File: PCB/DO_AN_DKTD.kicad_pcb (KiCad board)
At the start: 2 copper layers, 96 x 97.2 mm, 147 parts, among them IC1 RTC_DS3231M, J10 Jack-DC, J11 Conn_01x03_Pin, J12 Micro_SD_Card_Det1, J2 Conn_01x02, J3 Conn_01x04, J4 Conn_01x03, J5 Conn_01x02, J6 , J7 Conn_01x05_Male, J9 USB_C_Receptacle, Q1 NPN, Q10 P_Mosfet, Q2 NPN, Q3 NPN, Q4 NPN, Q5 NPN, Q6 NPN, Q7 NPN, Q8 NPN, Q9 N_Mosfet, SW1 RotaryEncoder_Switch, SW2 SW_Push, SW3 SW_Push, SW4 SW_Push, U1 AMS1117, U10 ESP-07, U2 74HC595, U3 PC817, U4 MOC3020M, U5 XL1509, U6 74HC595, U7 STM32F103C8Tx, U8 24C32N, U9 Ai-Thinker-Ra-02, Y1 Crystal_GND24_Small

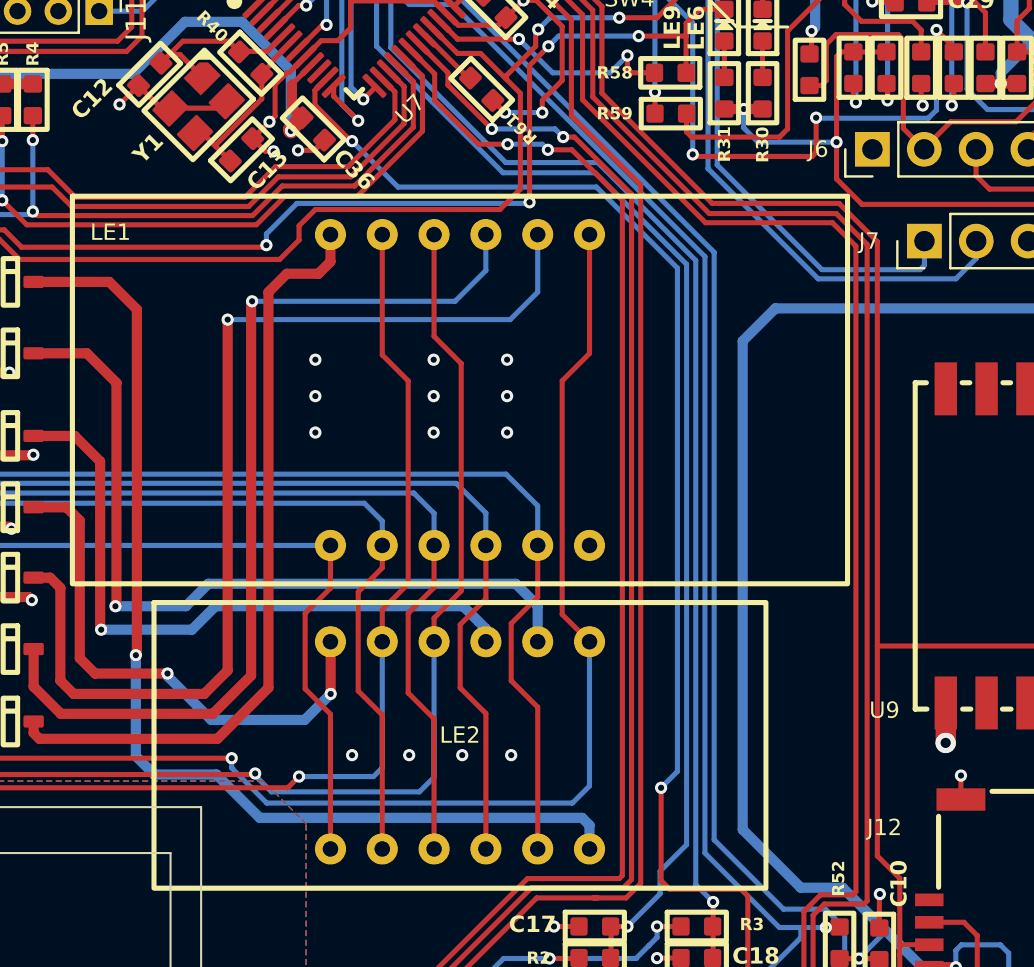
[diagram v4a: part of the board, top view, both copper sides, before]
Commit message: Update some footprints name
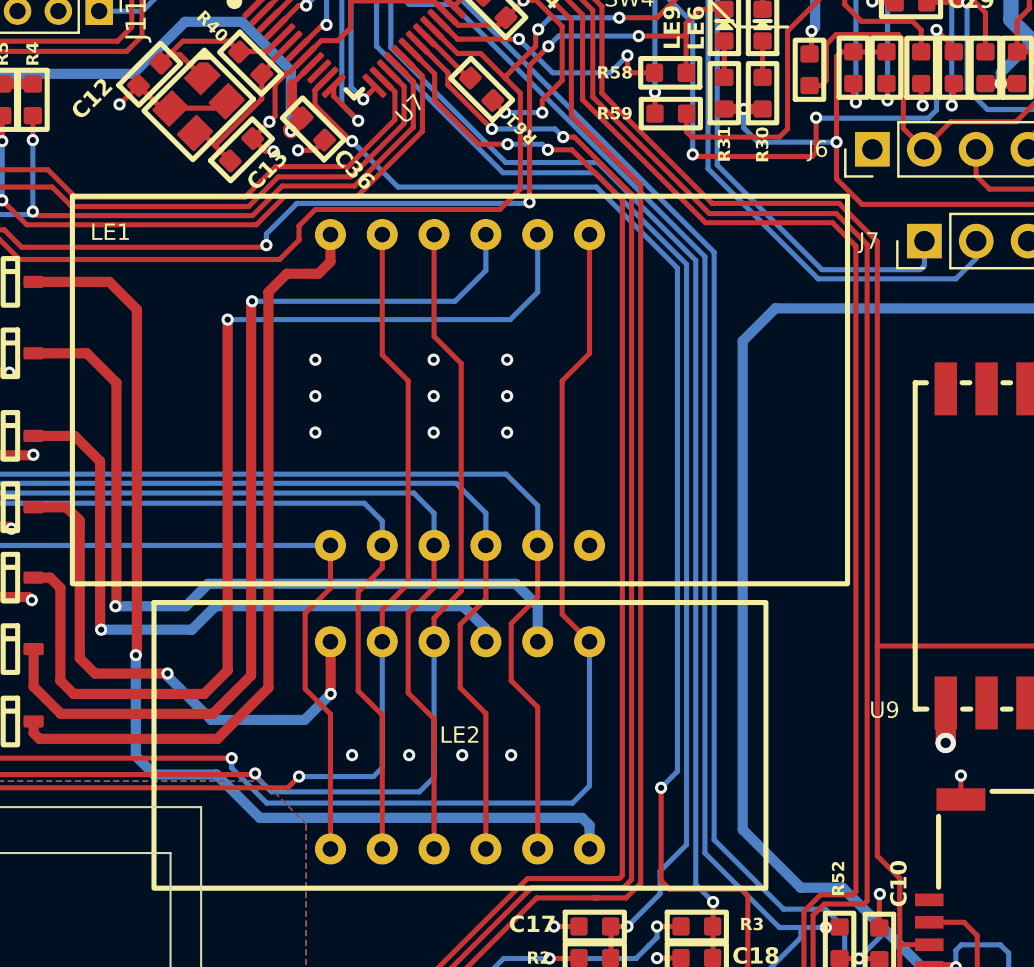
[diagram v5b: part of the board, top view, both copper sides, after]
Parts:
- J12: footprint IVS_FOOTPRINTS:MicroSD_Socket_9P -> IVS_FOOTPRINTS:Socket_MicroSD-9P
- Y1: footprint IVS_FOOTPRINTS:Crystal_3225_4P_3.2x2.6mm -> IVS_FOOTPRINTS:Crystal-SMD-4P-3.2x2.6mm-3225
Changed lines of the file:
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@@
   (net 133 "Net-(Q10-G)")
   (net 134 "/POWER/B")
-  (net 135 "Net-(IC1-VBAT)")
+  (net 135 "Net-(#FLG03-pwr)")
   (net 136 "/74HC595_HEADER_OUTPUT/LE2")
   (net 137 "/74HC595_HEADER_OUTPUT/LE1")
@@
       (net 2 "GND") (pinfunction "GND") (pintype "power_in"))
     (pad "14" smd roundrect (at 4.65 -1.905) (size 2.05 0.6) (layers "F.Cu" "F.Paste" "F.Mask") (roundrect_rratio 0.25)
-      (net 135 "Net-(IC1-VBAT)") (pinfunction "VBAT") (pintype "power_in"))
+      (net 135 "Net-(#FLG03-pwr)") (pinfunction "VBAT") (pintype "power_in"))
     (pad "15" smd roundrect (at 4.65 -3.175) (size 2.05 0.6) (layers "F.Cu" "F.Paste" "F.Mask") (roundrect_rratio 0.25)
       (net 57 "/74HC595_HEADER_OUTPUT/SHT31.SDA") (pinfunction "SDA") (pintype "bidirectional"))
@@
       (net 33 "/RTC_DS3231/Vbat") (pintype "passive"))
     (pad "3" smd roundrect (at 0 -1.1375 90) (size 1 0.6) (layers "F.Cu" "F.Paste" "F.Mask") (roundrect_rratio 0.15)
-      (net 135 "Net-(IC1-VBAT)") (pintype "passive"))
+      (net 135 "Net-(#FLG03-pwr)") (pintype "passive"))
     (model "${IOTVISION_3D}/MCU_SoC_Package/SOT23/SOT23-3.step"
       (offset (xyz 0 0 0.7))
@@
     )
   )
-  (footprint "IVS_FOOTPRINTS:Crystal_3225_4P_3.2x2.6mm" (layer "F.Cu")
+  (footprint "IVS_FOOTPRINTS:Crystal-SMD-4P-3.2x2.6mm-3225" (layer "F.Cu")
     (at 139.878858 78.023223 -135)
     (property "Sheetfile" "STM32.kicad_sch")
@@
     (property "ki_keywords" "quartz ceramic resonator oscillator")
     (attr smd)
-    (fp_text reference "Y1" (at 3.25 0.25 45 unlocked) (layer "F.SilkS")
-        (effects (font (size 0.8 0.8) (thickness 0.2) bold))
+    (fp_text reference "Y1" (at 3.25 0.25 -135 unlocked) (layer "F.SilkS") hide
+        (effects (font (size 0.8 0.8) (thickness 0.3) bold))
     )
-    (fp_text value "Crystal_GND24_Small" (at 3.11127 -4.525483 -45 unlocked) (layer "F.Fab")
+    (fp_text value "Crystal_GND24_Small" (at 0 1 -135 unlocked) (layer "F.Fab")
         (effects (font (size 1 1) (thickness 0.15)))
     )
@@
     (pad "4" smd roundrect (at -1.1 -0.85 225) (size 1.4 1.2) (layers "F.Cu" "F.Paste" "F.Mask") (roundrect_rratio 0.05)
       (net 2 "GND") (pinfunction "4") (pintype "passive"))
-    (model "${IOTVISION_3D}/Crystal/SMD/Crystal_SMD_5032-4Pin_5.0x3.2mm/Crystal_SMD_5032-4Pin_5.0x3.2mm.wrl"
+    (model "${IOTVISION_3D}/Crystal/SMD/Crystal_SMD_3225/3225 SMD Crystal Oscillator.STEP"
       (offset (xyz 0 0 0))
       (scale (xyz 1 1 1))
-      (rotate (xyz 0 0 0))
+      (rotate (xyz -90 0 0))
     )
   )
@@
     (fp_line (start 5.3 -3.35) (end 3.29 -5.3)
       (stroke (width 0.25) (type solid)) (layer "F.SilkS"))
-    (fp_arc (start -4.883987 5.298352) (mid -5.189989 5.16999) (end -5.303987 4.858352)
+    (fp_arc (start -4.883987 5.298352) (mid -5.189988 5.16999) (end -5.303987 4.858352)
       (stroke (width 0.25) (type solid)) (layer "F.SilkS"))
-    (fp_arc (start 3.4 -5.3) (mid 4.671188 -4.896237) (end 5.3 -3.72)
+    (fp_arc (start 3.4 -5.3) (mid 4.671185 -4.896237) (end 5.3 -3.72)
       (stroke (width 0.25) (type solid)) (layer "F.SilkS"))
     (fp_rect (start -5.65 -5.5) (end 5.75 5.65)
@@
     )
   )
-  (footprint "IVS_FOOTPRINTS:MicroSD_Socket_9P" (layer "F.Cu")
+  (footprint "IVS_FOOTPRINTS:Socket_MicroSD-9P" (layer "F.Cu")
     (at 186.9225 119.575 90)
     (property "Sheetfile" "MICRO_SD.kicad_sch")
@@
     (property "ki_keywords" "connector SD microsd")
     (attr smd)
-    (fp_text reference "J12" (at 6.125 -13.4225 180) (layer "F.SilkS")
-        (effects (font (size 0.8 0.8) (thickness 0.2)))
+    (fp_text reference "J12" (at 0 -0.35 90) (layer "F.SilkS") hide
+        (effects (font (size 0.8 0.8) (thickness 0.3)))
     )
     (fp_text value "Micro_SD_Card_Det1" (at 0 5.1 90) (layer "F.Fab")
@@
     (pad "10" smd rect (at 8.475 -0.425 90) (size 1.1 2.4) (layers "F.Cu" "F.Paste" "F.Mask")
       (net 2 "GND") (pinfunction "SHIELD") (pintype "passive"))
-    (model "${IOTVISION_3D}/Connector/MicroSDCardSocket/MicroSD_Socket.STEP"
+    (model "${IOTVISION_3D}/Connector/Socket/MicroSDCardSocket/MicroSD_Socket.STEP"
       (offset (xyz 0.3 3.5 0))
       (scale (xyz 1 1 1))
